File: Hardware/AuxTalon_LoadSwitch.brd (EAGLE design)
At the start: 70 x 35 mm, 64 parts, among them J1 CONN_AUX_M12_REMOTE, J2 CONN_AUX_M12_REMOTE, J3 CONN_AUX_M12_REMOTE, J4 CONN_TALON_REMOTE, U1 ADS1115, U11 MCP23018QFN, U16 MAX9064, U17 MAX9064, U18 SN74AUP1T87, U19 MAX9064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

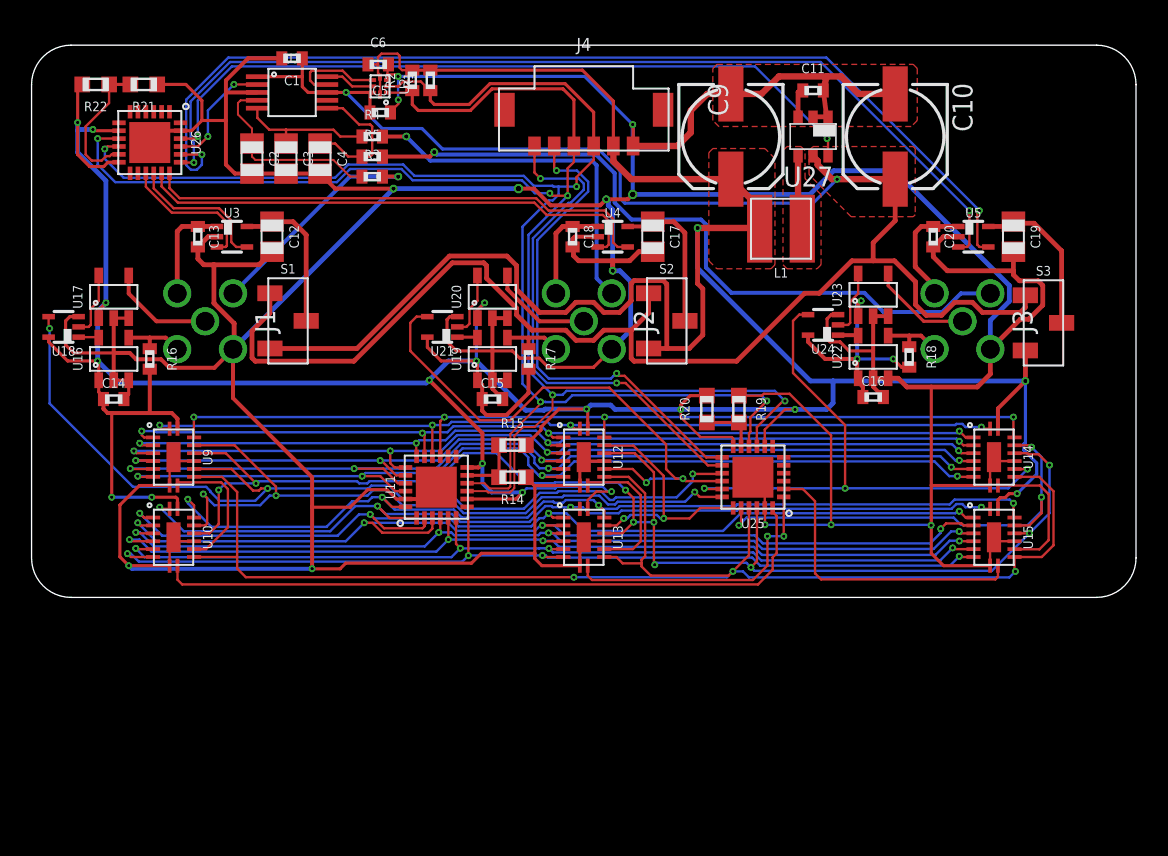
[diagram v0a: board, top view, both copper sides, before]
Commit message: Added ESD diodes, moved connector positioning
Added some ESD diodes on signal lines and changed positioning of connectors to restrict install to a single direction
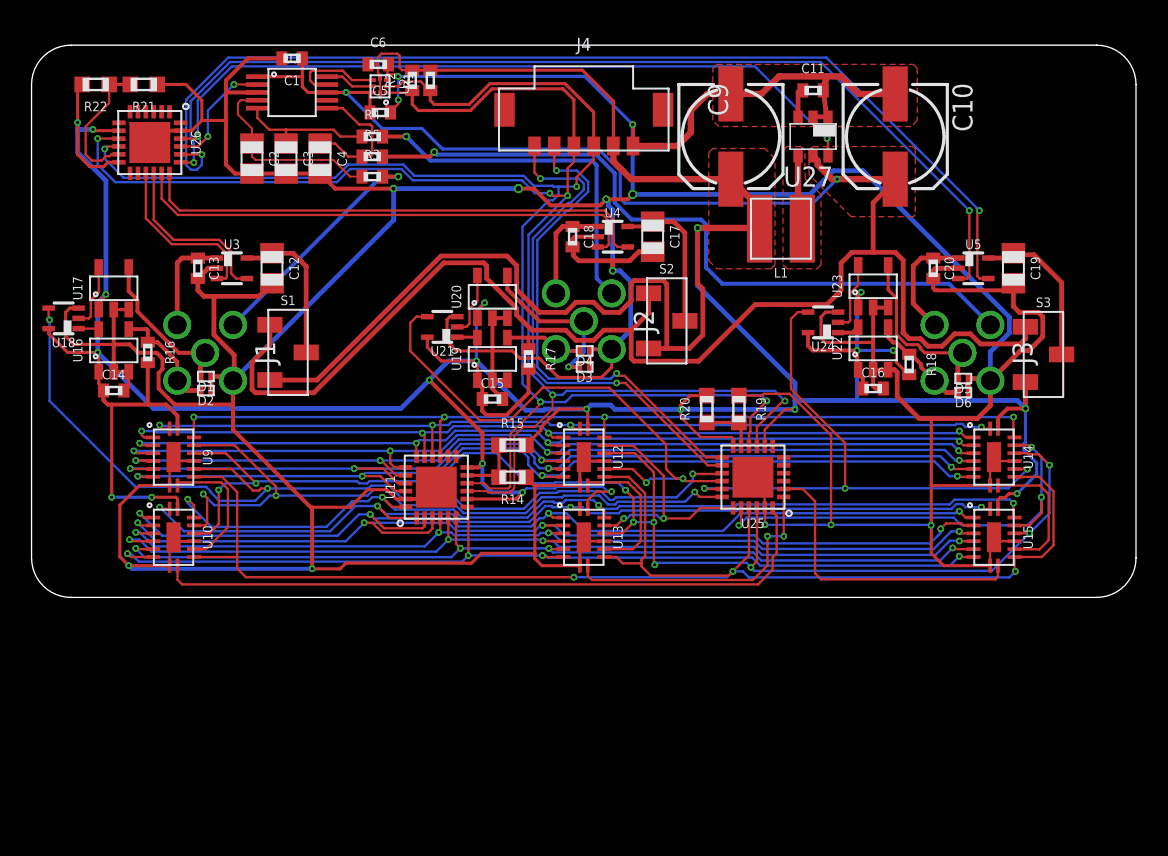
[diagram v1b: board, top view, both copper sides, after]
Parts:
- added D1, D2, D3, D4, D5, D6: 6V, bschulz:D0402
- moved S3 2.00 mm to (64.1, 15.4)
- moved C12 2.00 mm to (15.2, 20.9)
- moved C13 2.00 mm to (10.5, 20.9)
- moved C19 2.00 mm to (62.2, 20.9)
- moved C20 2.00 mm to (57.1, 20.9)
- moved J1 2.00 mm to (11.0, 15.5)
- moved J3 2.00 mm to (59.0, 15.5)
- moved S1 2.00 mm to (16.3, 15.5)
- moved U3 2.00 mm to (12.7, 20.9)
- moved U5 2.00 mm to (59.7, 20.9)
- moved C16 0.54 mm to (53.3, 13.2)
- moved U16 0.54 mm to (5.21, 15.7)
- moved C14 0.54 mm to (5.21, 13.1)
- moved U17 0.54 mm to (5.21, 19.6)
- moved U18 0.54 mm to (2.03, 17.7)
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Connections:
- net D1: now also D1.2
- net D2: now also D3.2
- net D3: now also D5.2
- net GND: now also D1.1, D2.1, D3.1, D4.1, D5.1, D6.1
- net OD1: now also D2.2
- net OD2: now also D4.2
- net OD3: now also D6.2
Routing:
- net GND: track 396.3 -> 408.7 mm
- net D3: track 6.42 -> 11.1 mm
- net 5V: track 129.3 -> 133.7 mm
- net D2: track 6.55 -> 10.5 mm, vias 0 -> 1
- net D1: track 6.71 -> 10.0 mm
- net OD1: track 4.08 -> 7.29 mm
- net OD3: track 4.00 -> 6.62 mm
- net PORT3_EN: track 65.8 -> 67.8 mm
- net PORT1_EN: track 9.20 -> 11.2 mm
- net !PORT1_FAULT: track 9.07 -> 11.1 mm
- net !PORT3_FAULT: track 62.0 -> 64.0 mm
- net OD2: track 4.07 -> 5.59 mm
- net 3V3: track 306.6 -> 307.5 mm
- net AIN1: track 14.5 -> 15.4 mm

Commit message: Layout, gerbers, and BoM for v0.0 - sent to fab
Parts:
- R14, R20: value (none) -> 82k
- R15, R19: value (none) -> 62k
- R21: value (none) -> 10k
- R22: value (none) -> 150k
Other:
- board text added: "3V3"
- board text added: "5V"
- board text added: "GEMS Sensing"
- board text added: "Port1"
- board text added: "Port2"
- board text added: "Port3"
- board text added: "Talon - Aux v0.0 - LS Bobby Schulz"

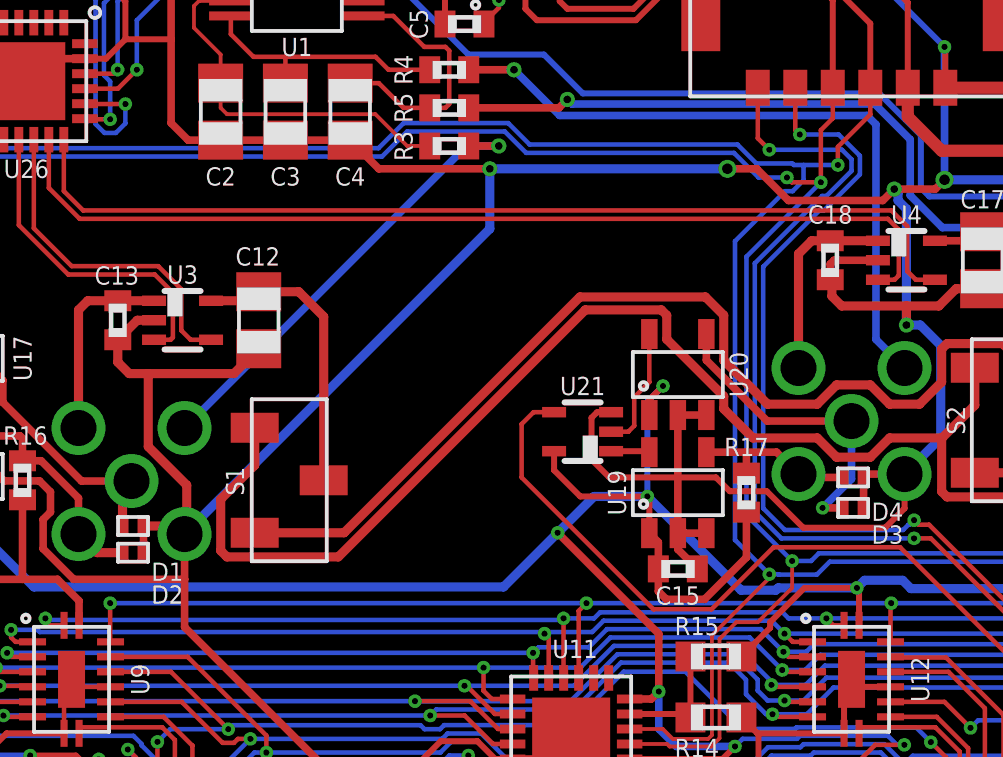
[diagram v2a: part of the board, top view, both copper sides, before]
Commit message: v0.1 Updates - Added EEPROM
Added EEPROM to board
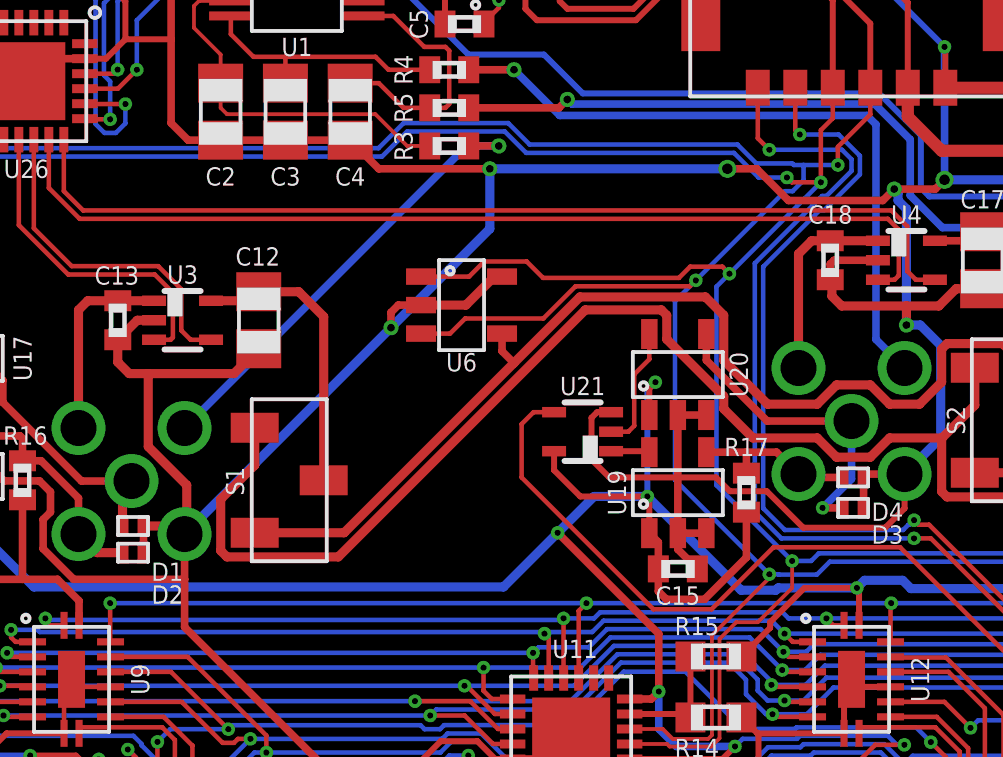
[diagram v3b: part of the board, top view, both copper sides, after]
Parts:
- added U6: 24AA02SOT23, bschulz:SOT23-5
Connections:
- net 3V3: now also U6.4
- net GND: now also U6.2, U6.5
- net SCL: now also U6.1
- net SDA: now also U6.3
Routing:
- net SCL: track 97.9 -> 109.6 mm, vias 5 -> 6
- net SDA: track 95.9 -> 107.4 mm, vias 4 -> 5
- net GND: track 408.7 -> 413.4 mm, vias 13 -> 14
- net 3V3: track 307.5 -> 308.7 mm
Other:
- board text added: "SN"
- board text added: "Talon - Aux v0.1 - LS Bobby Schulz"
- board text removed: "Talon - Aux v0.0 - LS Bobby Schulz"

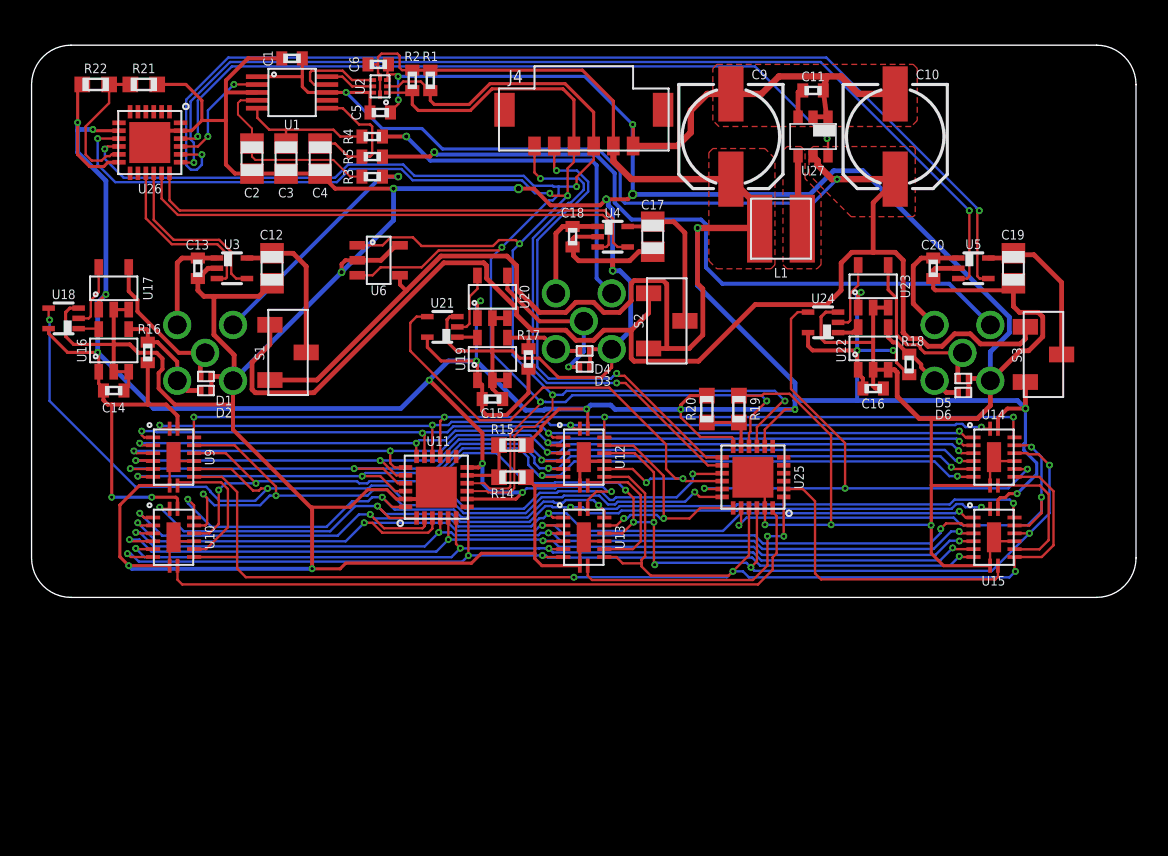
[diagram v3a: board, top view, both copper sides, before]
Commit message: v1.0 Updates
Added voltage sensing for ports, swapped 5V converter, sent v1.0 to fab
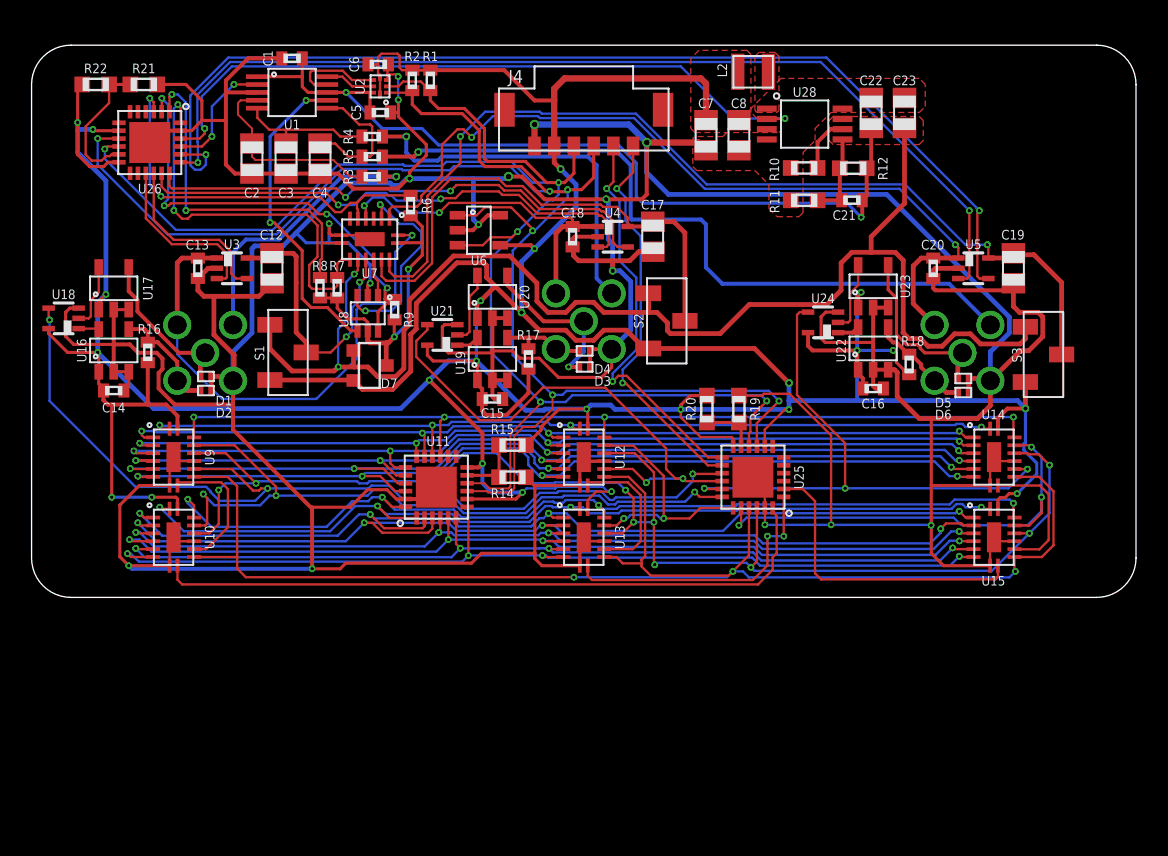
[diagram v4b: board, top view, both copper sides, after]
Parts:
- removed C10, C9: 68uF, bschulz_passives:153CLV-0605
- removed C11: 0.1uF, bschulz_passives:C0402
- removed L1: 22uH, bschulz:WE-TPC(3.8X3.8)
- removed U27: AP1603, bschulz:TSOT23-6_DDC
- added C21: (no value), bschulz_passives:C0402
- added C22, C23: 22uF, bschulz_passives:C0805
- added C7, C8: 10uF, bschulz_passives:C0805
- added D7: (no value), bschulz:SOT23-3
- added L2: (no value), bschulz:WE-MAPI(2.5X2)
- added R10: 68k, bschulz_passives:R0603
- added R11: 100k, bschulz_passives:R0603
- added R12: 750k, bschulz_passives:R0603
- added R6, R7, R8, R9: 100k, bschulz_passives:R0402
- added U28: PAM2401MSOP, bschulz:MSOP_8
- added U7: 74HC4852, bschulz:VQFN-16
- added U8: SN74LVC1G3157SC70, bschulz:DCK_R-PDSO-G6
- moved U6 6.63 mm to (28.4, 23.3)
- moved U21 0.51 mm to (26.0, 16.6)
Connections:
- removed net N$15: C11.1, U27.3
- removed net N$17: L1.2, U27.4
- removed net N$26: U25.3
- removed net N$29: U25.6
- removed net N$30: U25.7
- removed net VREF: U1.7
- new net BUS_SENSE: U1.7, U8.4
- new net MUX_EN: R6.1, U26.3, U7.6
- new net MUX_SEL0: R7.1, U26.24, U7.10
- new net MUX_SEL1: R8.1, U26.1, U7.9
- new net N$1: U7.3, U8.3
- new net N$18: L2.P$2, U28.1
- new net N$2: R10.2, U28.6
- new net N$3: C21.2, R11.2, R12.1, U28.5
- new net N$38: U7.13, U8.1
- new net VMUX: D7.3, R6.2, R7.2, R8.2, R9.2, U7.16, U8.5
- net 3V3: now also C7.1, C8.1, D7.2, J4.2, L2.P$1, U28.3; no longer C9.+, J4.5, L1.1
- net 5V: now also C21.1, C22.1, C23.1, D7.1, R12.2, U28.7, U7.11; no longer C10.+, U27.5
- net 5V_EN: now also U28.2; no longer U27.6
- net GND: now also C22.2, C23.2, C7.2, C8.2, J4.1, R10.1, R11.1, U28.4, U28.8, U7.8, U7.EP, U8.2; no longer C10.-, C11.2, C9.-, J4.6, U27.1, U27.2
- net GPIOA: now also J4.6; no longer J4.1
- net GPIOB: now also J4.5; no longer J4.2
- net MUX_SEL2: now also R9.1, U26.2, U8.6; no longer U25.5
- net SCL: now also J4.4; no longer J4.3
- net SDA: now also J4.3; no longer J4.4
- net VPORT1_IN: now also U7.12
- net VPORT1_OUT: now also U7.1
- net VPORT2_IN: now also U7.14
- net VPORT2_OUT: now also U7.5
- net VPORT3_IN: now also U7.15
- net VPORT3_OUT: now also U7.2
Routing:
- net VPORT3_IN: track 10.2 -> 61.0 mm, vias 0 -> 2
- net VPORT3_OUT: track 7.36 -> 52.4 mm, vias 0 -> 2
- net MUX_SEL2: track 0.00 -> 28.6 mm, vias 0 -> 4
- net VPORT1_OUT: track 6.58 -> 33.1 mm, vias 0 -> 1
- net MUX_SEL0: track 0.00 -> 26.0 mm, vias 0 -> 2
- net MUX_EN: track 0.00 -> 25.2 mm, vias 0 -> 2
- net VPORT2_IN: track 9.63 -> 33.1 mm
- net MUX_SEL1: track 0.00 -> 22.8 mm, vias 0 -> 2
- net BUS_SENSE: track 0.00 -> 20.1 mm, vias 0 -> 2
- net VMUX: track 0.00 -> 19.9 mm, vias 0 -> 2
- net VPORT2_OUT: track 6.63 -> 22.5 mm, vias 0 -> 2
- net N$1: track 0.00 -> 12.9 mm, vias 0 -> 2
- net 3V3: track 308.7 -> 298.6 mm, vias 21 -> 24
- net 5V: track 133.7 -> 142.2 mm, vias 2 -> 4
- net VPORT1_IN: track 9.68 -> 18.1 mm, vias 0 -> 2
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- added copper zone on layer 1, net N$18
- removed copper zone on layer 1, net N$17
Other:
- board text added: "Talon - Aux v1.0 - LS Bobby Schulz"
- board text removed: "Talon - Aux v0.1 - LS Bobby Schulz"

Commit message: Update part val, generated BoM for v1.0
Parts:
- L2: value (none) -> 4.7uH
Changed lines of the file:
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@@
 <attribute name="VALUE_PART" value="" x="48.967" y="27.217" size="1.778" layer="27" display="off"/>
 </element>
-<element name="L2" library="bschulz" package="WE-MAPI(2.5X2)" value="" x="45.729" y="33.313" smashed="yes">
+<element name="L2" library="bschulz" package="WE-MAPI(2.5X2)" value="4.7uH" x="45.729" y="33.313" smashed="yes">
 <attribute name="NAME" x="43.776" y="33.41" size="0.6096" layer="25" font="vector" ratio="15" rot="R90" align="center"/>
 </element>

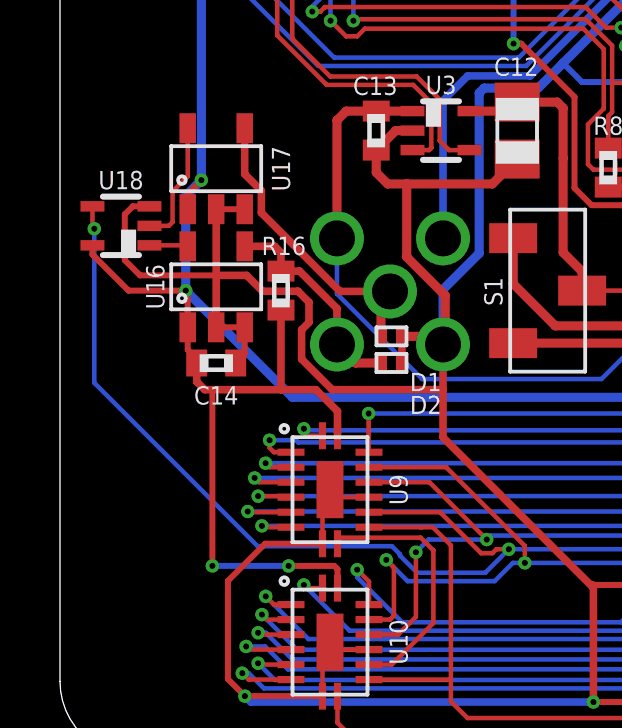
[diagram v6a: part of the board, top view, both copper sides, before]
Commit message: v1.1 update
Moved via
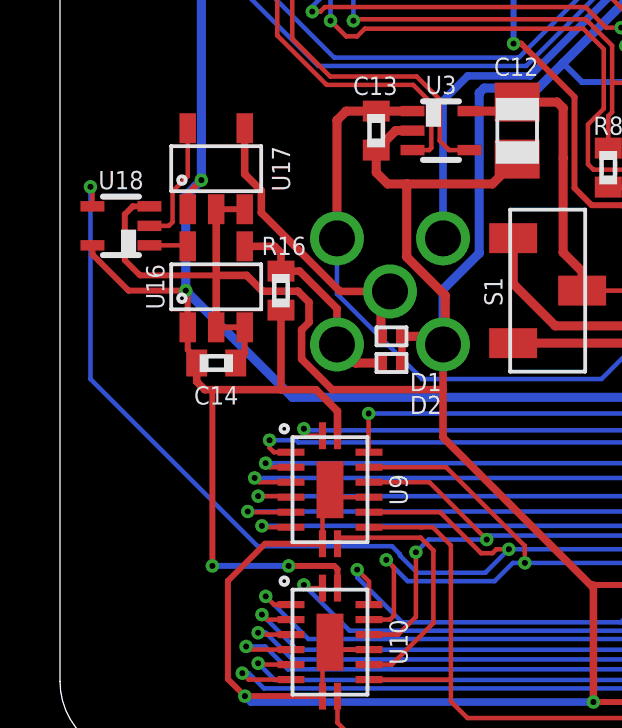
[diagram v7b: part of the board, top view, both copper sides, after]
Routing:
- net OUT1: track 59.1 -> 60.5 mm
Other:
- board text added: "Talon - Aux v1.1 - LS Bobby Schulz"
- board text removed: "Talon - Aux v1.0 - LS Bobby Schulz"
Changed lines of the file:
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@@
 <wire x1="2.5" y1="35" x2="0" y2="32.5" width="0" layer="20" curve="90"/>
 <text x="58.547" y="31.369" size="1.27" layer="51" font="vector" ratio="15" align="center-left">Talon - Aux
-v1.0 - LS
+v1.1 - LS
 Bobby Schulz</text>
 <text x="53.891" y="25.241" size="1.778" layer="51" font="vector" ratio="15" align="center-left">GEMS Sensing</text>
@@
 <wire x1="14.1764" y1="6.1214" x2="11.90328125" y2="6.1214" width="0.1524" layer="16"/>
 <wire x1="11.06471875" y1="7.0072" x2="6.5868" y2="7.0072" width="0.1524" layer="16"/>
-<wire x1="6.5868" y1="7.0072" x2="1.143" y2="12.451" width="0.1524" layer="16"/>
-<wire x1="1.143" y1="12.451" x2="1.143" y2="17.5894" width="0.1524" layer="16"/>
-<via x="1.143" y="17.5894" extent="1-16" drill="0.2"/>
-<wire x1="1.143" y1="17.5894" x2="1.082" y2="17.6504" width="0.1524" layer="1"/>
-<wire x1="1.082" y1="17.6504" x2="1.082" y2="18.335" width="0.1524" layer="1"/>
+<wire x1="6.5868" y1="7.0072" x2="1.016" y2="12.578" width="0.1524" layer="16"/>
+<wire x1="1.016" y1="12.578" x2="1.016" y2="18.9864" width="0.1524" layer="16"/>
+<via x="1.016" y="18.9864" extent="1-16" drill="0.2"/>
+<wire x1="1.016" y1="18.9864" x2="1.082" y2="18.9204" width="0.1524" layer="1"/>
+<wire x1="1.082" y1="18.335" x2="1.082" y2="18.9204" width="0.1524" layer="1"/>
 <wire x1="21.534725" y1="7.085" x2="22.65645625" y2="7.085" width="0.1524" layer="16"/>
 <wire x1="23.54385625" y1="6.1976" x2="22.65645625" y2="7.085" width="0.1524" layer="16"/>

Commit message: Prelim v1.3 updates
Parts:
- added C10, C11, C9: (no value), bschulz_passives:C0402
- added R13, R23, R24: (no value), bschulz_passives:R0402
- moved S2 1.27 mm to (41.5, 17.5)
- moved S3 1.27 mm to (65.4, 15.4)
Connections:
- net D1: now also R13.2
- net D2: now also R23.2
- net D3: now also R24.2
- net GND: now also C10.2, C11.2, C9.2, R13.1, R23.1, R24.1
- net OD1: now also C11.1
- net OD2: now also C10.1
- net OD3: now also C9.1
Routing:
- net D3: track 11.1 -> 14.9 mm
- net GND: track 410.3 -> 413.9 mm
- net 3V3: track 298.6 -> 296.7 mm
- net 5V: track 142.2 -> 140.9 mm
- net VPORT2_IN: track 33.1 -> 33.6 mm
- net VPORT3_IN: track 61.0 -> 61.6 mm
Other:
- board text added: "Talon - Aux v1.3 - LS Bobby Schulz"
- board text removed: "Talon - Aux v1.1 - LS Bobby Schulz"
